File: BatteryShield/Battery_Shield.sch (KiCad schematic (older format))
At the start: 0 parts

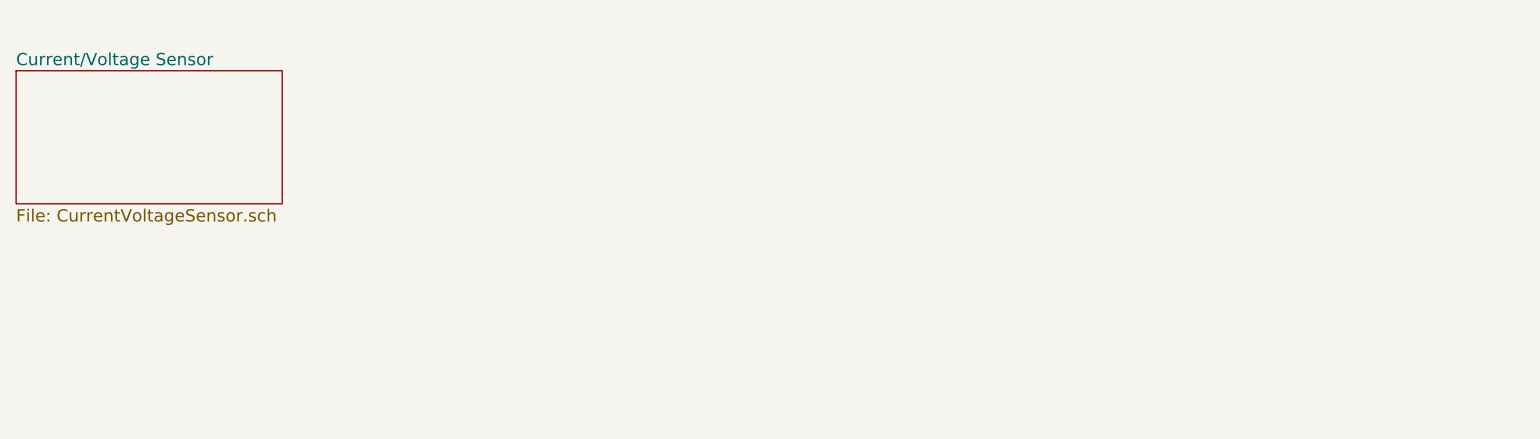
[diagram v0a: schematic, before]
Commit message: Fixing folder/adding schematics to hierarchal sheet
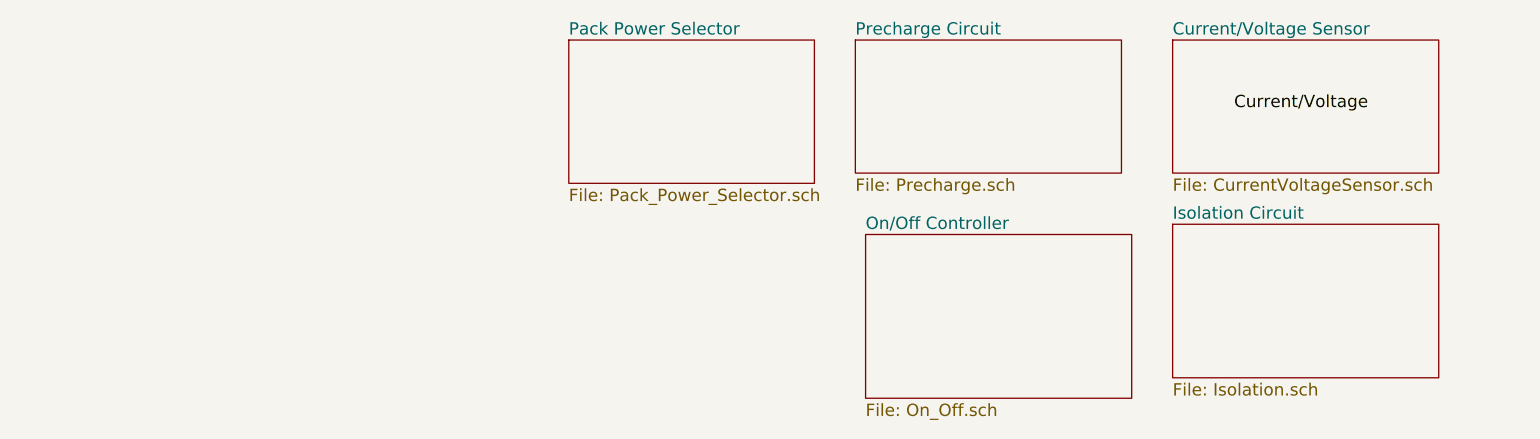
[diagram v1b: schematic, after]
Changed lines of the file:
@@
 $Descr A4 11693 8268
 encoding utf-8
-Sheet 1 2
+Sheet 1 5
 Title ""
 Date ""
@@
 $EndDescr
 $Sheet
-S 1650 1950 1300 650
+S 7300 1800 1300 650
 U 5A64EF94
 F0 "Current/Voltage Sensor" 60
 F1 "CurrentVoltageSensor.sch" 60
 $EndSheet
+Text Label 7600 2150 0    60   ~ 0
+Current/Voltage
+$Sheet
+S 7300 2700 1300 750
+U 5A668B9B
+F0 "Isolation Circuit" 60
+F1 "Isolation.sch" 60
+$EndSheet
+$Sheet
+S 5750 1800 1300 650
+U 5A668BC0
+F0 "Precharge Circuit" 60
+F1 "Precharge.sch" 60
+$EndSheet
+$Sheet
+S 5800 2750 1300 800
+U 5A668BD8
+F0 "On/Off Controller" 60
+F1 "On_Off.sch" 60
+$EndSheet
+$Sheet
+S 4350 1800 1200 700
+U 5A668BFB
+F0 "Pack Power Selector" 60
+F1 "Pack_Power_Selector.sch" 60
+$EndSheet
 $EndSCHEMATC

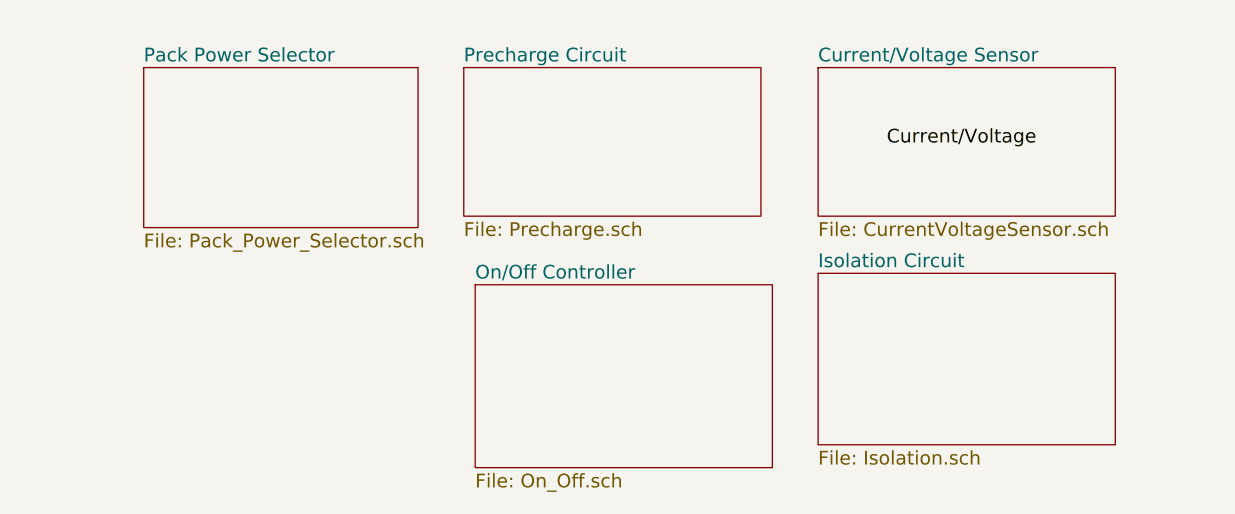
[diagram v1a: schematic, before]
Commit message: Directory/.pro cleanup
Cleanup of .pro and removed CurrentVoltageSensor.pro
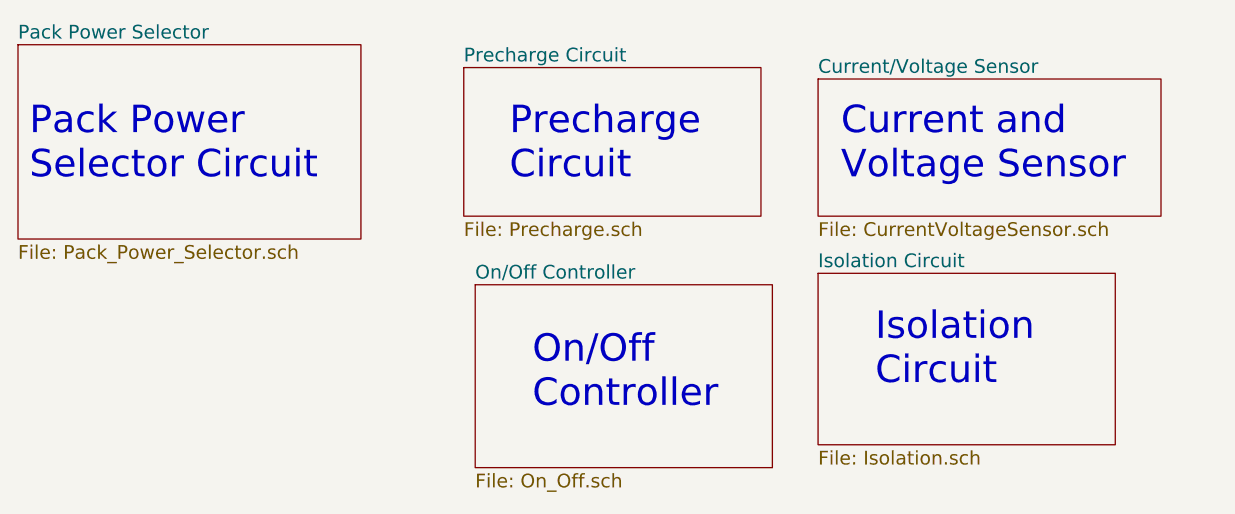
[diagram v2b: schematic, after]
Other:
- note added: "Current and \nVoltage Sensor"
- note added: "Isolation\nCircuit"
- note added: "On/Off\nController"
- note added: "Pack Power\nSelector Circuit"
- note added: "Precharge\nCircuit"
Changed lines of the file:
@@
 LIBS:contrib
 LIBS:valves
-LIBS:mocd207m
-LIBS:symbols
 LIBS:Battery_Shield-cache
 EELAYER 25 0
@@
 $Descr A4 11693 8268
 encoding utf-8
-Sheet 1 5
+Sheet 1 6
 Title ""
 Date ""
@@
 $EndDescr
 $Sheet
-S 7300 1800 1300 650
+S 7300 1850 1500 600
 U 5A64EF94
 F0 "Current/Voltage Sensor" 60
 F1 "CurrentVoltageSensor.sch" 60
 $EndSheet
-Text Label 7600 2150 0    60   ~ 0
-Current/Voltage
 $Sheet
 S 7300 2700 1300 750
@@
 $EndSheet
 $Sheet
-S 4350 1800 1200 700
+S 3800 1700 1500 850
 U 5A668BFB
 F0 "Pack Power Selector" 60
 F1 "Pack_Power_Selector.sch" 60
 $EndSheet
+Text Notes 7400 2300 0    120  ~ 0
+Current and \nVoltage Sensor
+Text Notes 7550 3200 0    120  ~ 0
+Isolation\nCircuit
+Text Notes 6050 3300 0    120  ~ 0
+On/Off\nController
+Text Notes 5950 2300 0    120  ~ 0
+Precharge\nCircuit
+Text Notes 3850 2300 0    120  ~ 0
+Pack Power\nSelector Circuit
 $EndSCHEMATC

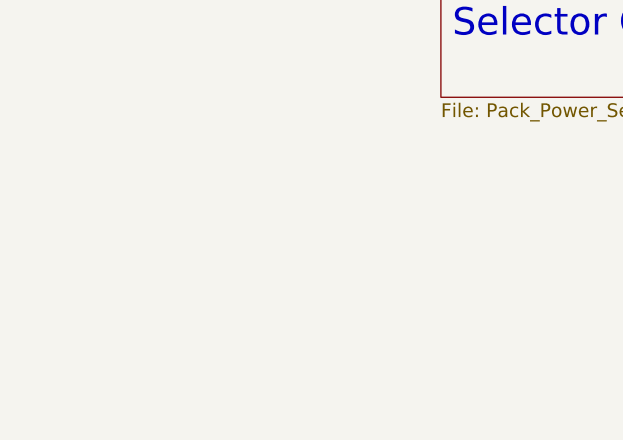
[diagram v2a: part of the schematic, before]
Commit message: Adding temperature sensor schematic
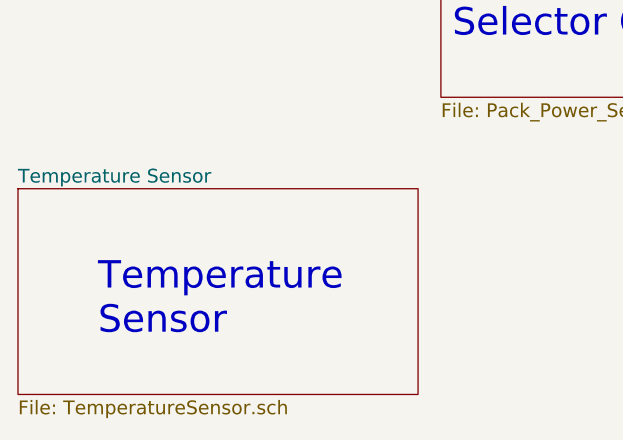
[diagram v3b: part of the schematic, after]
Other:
- note added: "Temperature\nSensor"
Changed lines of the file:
@@
 EESchema Schematic File Version 2
+LIBS:adc081c021
 LIBS:power
 LIBS:device
@@
 $Descr A4 11693 8268
 encoding utf-8
-Sheet 1 6
+Sheet 1 7
 Title ""
 Date ""
@@
 Text Notes 3850 2300 0    120  ~ 0
 Pack Power\nSelector Circuit
+$Sheet
+S 1950 2950 1750 900
+U 5A767D76
+F0 "Temperature Sensor" 60
+F1 "TemperatureSensor.sch" 60
+$EndSheet
+Text Notes 2300 3600 0    120  ~ 0
+Temperature\nSensor
 $EndSCHEMATC

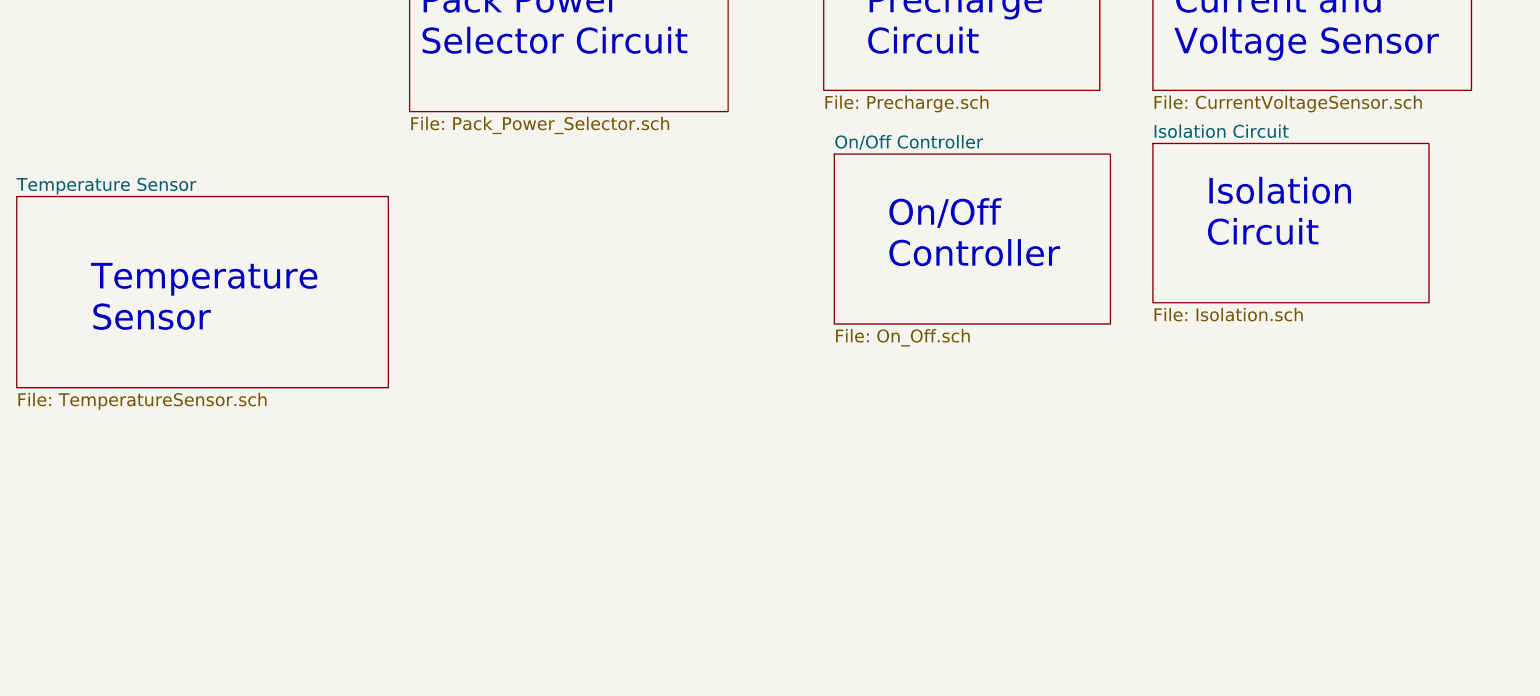
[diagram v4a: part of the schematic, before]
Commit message: 5V + 3.3V Regulators + Folder cleanup
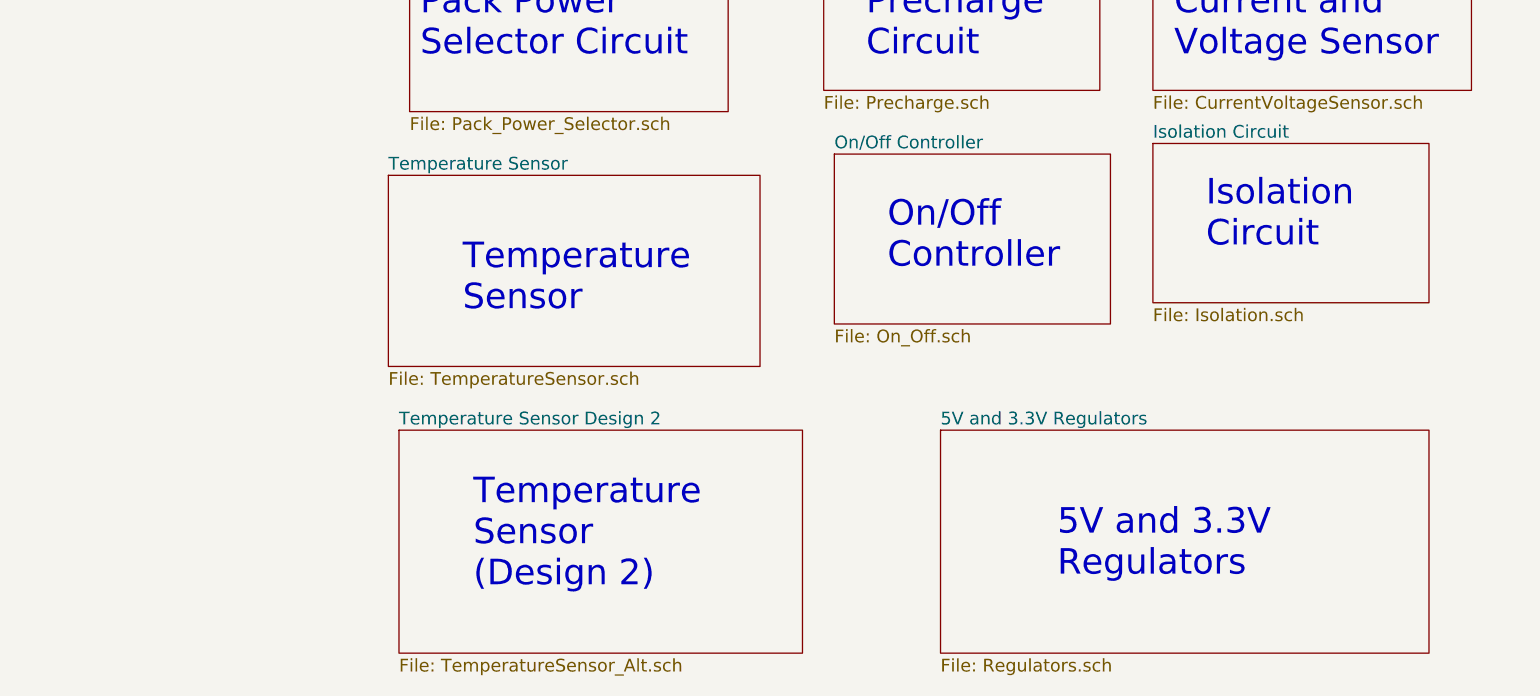
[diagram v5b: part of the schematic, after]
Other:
- note added: "5V and 3.3V\nRegulators"
- note added: "Temperature\nSensor\n(Design 2)"
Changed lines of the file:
@@
 LIBS:valves
 LIBS:LTC4151IMS-1-PBF
+LIBS:sensors
 LIBS:Battery_Shield-cache
 EELAYER 25 0
@@
 $Descr A4 11693 8268
 encoding utf-8
-Sheet 1 7
+Sheet 1 9
 Title ""
 Date ""
@@
 Pack Power\nSelector Circuit
 $Sheet
-S 1950 2950 1750 900
+S 3700 2850 1750 900
 U 5A767D76
 F0 "Temperature Sensor" 60
 F1 "TemperatureSensor.sch" 60
 $EndSheet
-Text Notes 2300 3600 0    120  ~ 0
+Text Notes 4050 3500 0    120  ~ 0
 Temperature\nSensor
+$Sheet
+S 3750 4050 1900 1050
+U 5A8239AC
+F0 "Temperature Sensor Design 2" 60
+F1 "TemperatureSensor_Alt.sch" 60
+$EndSheet
+Text Notes 4100 4800 0    120  ~ 0
+Temperature\nSensor\n(Design 2)
+$Sheet
+S 6300 4050 2300 1050
+U 5A86217E
+F0 "5V and 3.3V Regulators" 60
+F1 "Regulators.sch" 60
+$EndSheet
+Text Notes 6850 4750 0    120  ~ 0
+5V and 3.3V\nRegulators
 $EndSCHEMATC

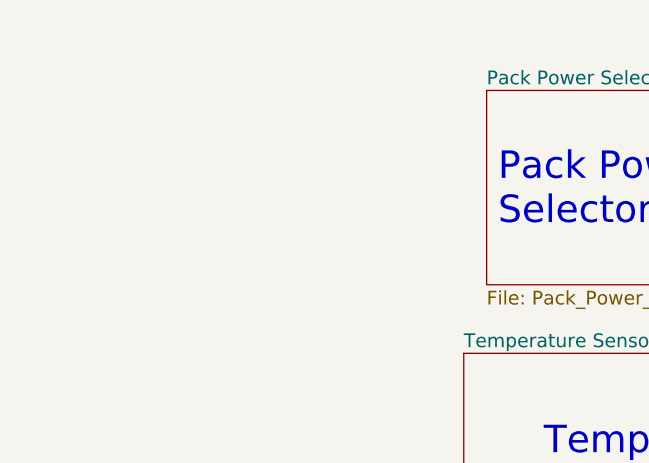
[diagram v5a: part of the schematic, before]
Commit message: Revised Power Pack Circuits
Also added an alternative power select circuit using power FETs
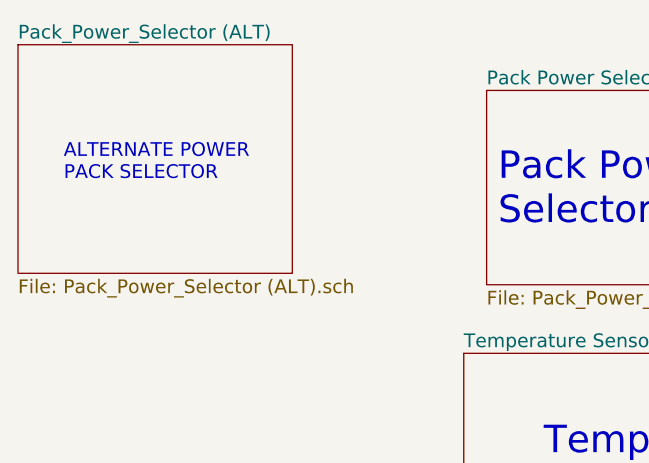
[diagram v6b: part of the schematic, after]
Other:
- note added: "ALTERNATE POWER\nPACK SELECTOR\n"
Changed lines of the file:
@@
 $Descr A4 11693 8268
 encoding utf-8
-Sheet 1 9
+Sheet 1 10
 Title ""
 Date ""
@@
 Text Notes 6850 4750 0    120  ~ 0
 5V and 3.3V\nRegulators
+$Sheet
+S 1750 1500 1200 1000
+U 5B0DE919
+F0 "Pack_Power_Selector (ALT)" 60
+F1 "Pack_Power_Selector (ALT).sch" 60
+$EndSheet
+Text Notes 1950 2100 0    60   ~ 0
+ALTERNATE POWER\nPACK SELECTOR\n
 $EndSCHEMATC
